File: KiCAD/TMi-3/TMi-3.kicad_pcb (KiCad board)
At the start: 2 copper layers, 50 x 160 mm, 41 parts, among them J1 MJ-3536NG, J2 MJ-3536NG, J3 MJ-3536NG, J4 MJ-3536NG, J5 NMJ4HFD3, J6 NMJ4HFD3, J7 NMJ4HFD3, J8 NMJ4HFD3, J9 Barrel_Jack_Switch, Q1 IRLZ44N, Q2 IRLZ44N, Q3 IRLZ44N, Q4 IRLZ44N

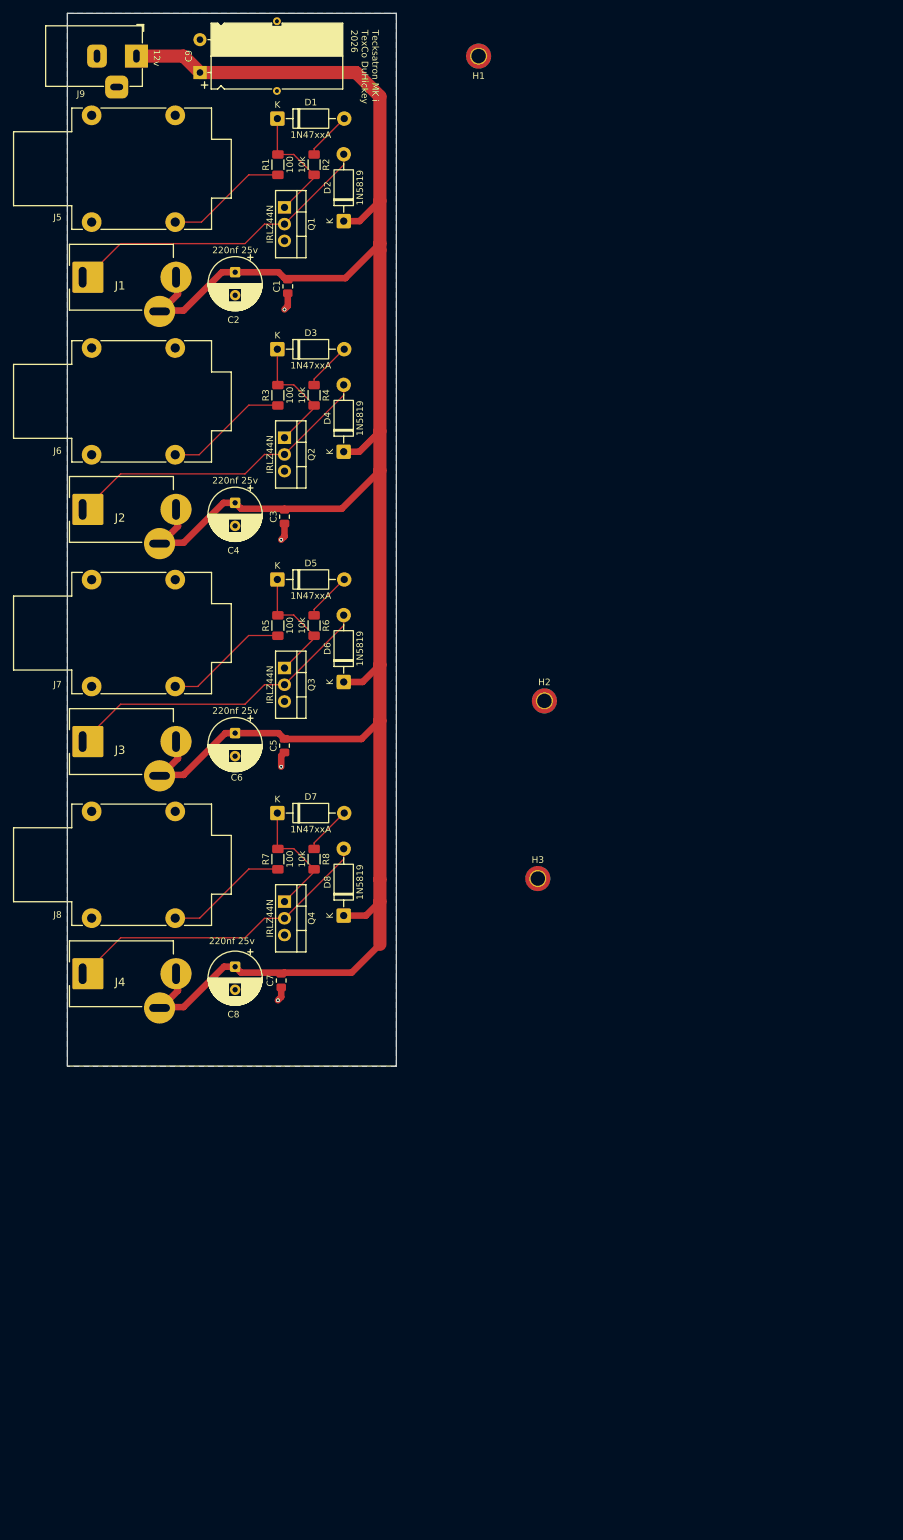
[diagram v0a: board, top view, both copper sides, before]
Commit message: Snapshot: MagnetPCB/TMi-3 KiCAD work, journal, TouchOSC, archive Additive1
Last state of this repo before its history continues in la-harpe-eliane.
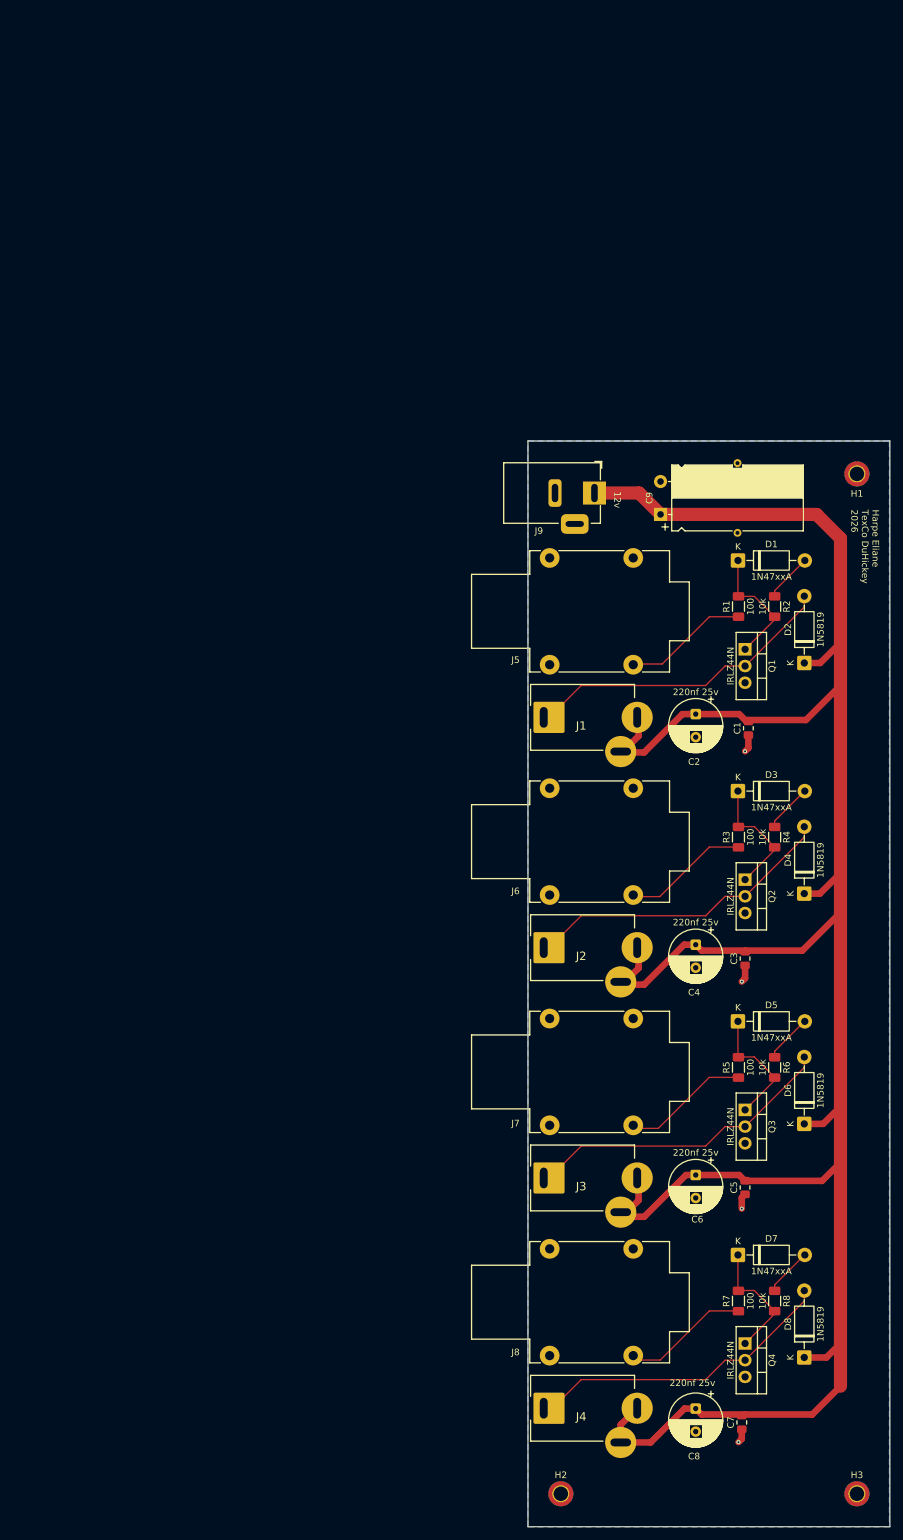
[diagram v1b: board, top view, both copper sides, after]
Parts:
- moved H2 120.5 mm to (105.0, 260.0)
- moved H3 105.3 mm to (150.0, 260.0)
- moved C2 97.0 mm to (125.5, 141.5)
- moved D4 97.0 mm to (142.0, 168.8)
- moved C1 97.0 mm to (133.5, 143.7)
- moved C3 97.0 mm to (133.0, 178.7)
- moved C4 97.0 mm to (125.5, 176.6)
- moved C5 97.0 mm to (133.0, 213.5)
- moved C6 97.0 mm to (125.5, 211.6)
- moved C7 97.0 mm to (132.5, 249.2)
- moved C8 97.0 mm to (125.5, 247.1)
- moved C9 97.0 mm to (120.1, 111.2)
- moved D1 97.0 mm to (131.9, 118.2)
- moved D2 97.0 mm to (142.0, 133.7)
- moved D3 97.0 mm to (131.9, 153.2)
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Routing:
- net +12V: track 371.7 -> 372.3 mm
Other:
- board size 50 x 160 mm -> 55 x 165 mm
- board text added: "Harpe Eliane TexCo DuHickey 2026"
- board text removed: "Tecksatron MK i TexCo DuHickey 2026"
